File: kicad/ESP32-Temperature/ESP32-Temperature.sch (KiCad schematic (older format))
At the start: 5 parts

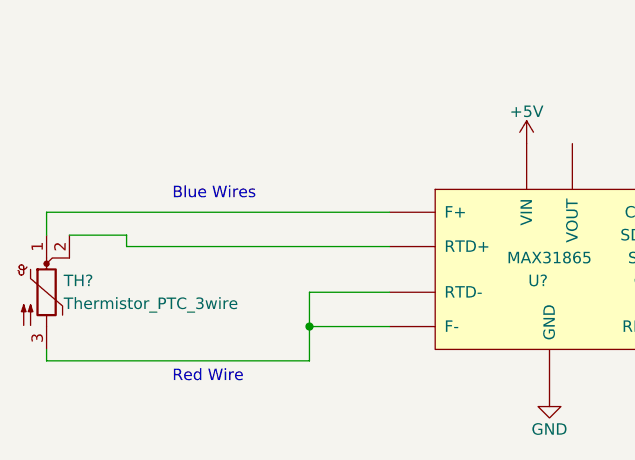
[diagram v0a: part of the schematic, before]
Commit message: change red/blue
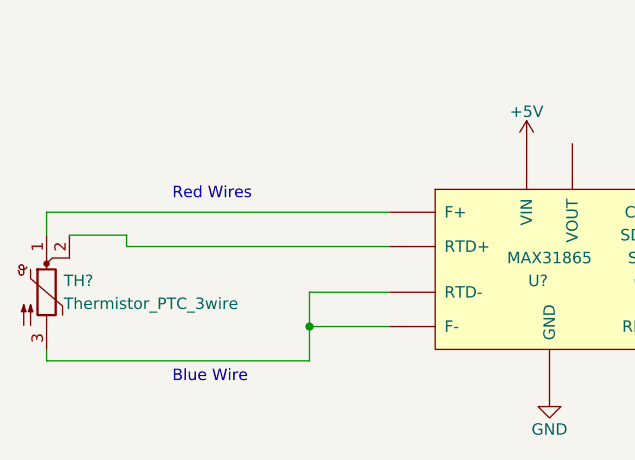
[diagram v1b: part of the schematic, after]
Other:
- note added: "Blue Wire"
- note added: "Red Wires"
- note removed: "Blue Wires"
- note removed: "Red Wire"
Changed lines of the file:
@@
 	3650 3300 4250 3300
 Text Notes 3300 5900 0    50   ~ 0
-Red Wire
+Blue Wire
 Text Notes 3300 5100 0    50   ~ 0
-Blue Wires
+Red Wires
 $Comp
 L power:GND #PWR?
